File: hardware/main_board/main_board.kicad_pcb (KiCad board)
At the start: 2 copper layers, 14 parts, among them J100 2x10 Male Pins, J2 2x10 Male Pins, J4 2x10 Male Pins, J5 2x10 Male Pins, J6 2x10 Male Pins, J7 2x10 Male Pins, U1 M0G3507QDGS32RQ1, U2 HiLetGo_ST7735R

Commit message: drew schematic
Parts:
- removed J100: 2x10 Male Pins, Connector_PinSocket_2.54mm:PinSocket_2x10_P2.54mm_Vertical
- removed TP1, TP110, TP2, TP3, TP4, TP5: GND, SamacSys_Parts:bettertestpoint2
- added C1: 0.47uF, Capacitor_SMD:C_0805_2012Metric, F.Cu at (139.0, 94.9)
- added C10: 1u, Capacitor_SMD:C_0805_2012Metric, F.Cu at (142.1, 53.9)
- added C11: 0u33, Capacitor_SMD:C_0805_2012Metric, F.Cu at (142.1, 56.9)
- added C12: 1u, Capacitor_SMD:C_0805_2012Metric, F.Cu at (142.1, 59.9)
- added C3: 10nF, Capacitor_SMD:C_0805_2012Metric, F.Cu at (139.0, 97.9)
- added C4: 10uF, Capacitor_SMD:C_0805_2012Metric, F.Cu at (139.0, 100.9)
- added C5: 0.1uF, Capacitor_SMD:C_0805_2012Metric, F.Cu at (139.0, 103.9)
- added D1: RUN_LED, 445L:LED_D5.0mm, F.Cu at (143.7, 97.2)
- added D2: PWR_LED, 445L:LED_D5.0mm, F.Cu at (151.2, 97.2)
- added IC2: LM4890M_NOPB, 445L:ti_LM4890M_NOPB, F.Cu at (148.6, 55.6)
- added J1: Conn_01x06_Pin, Connector_PinHeader_2.54mm:PinHeader_1x06_P2.54mm_Vertical, F.Cu at (143.5, 103.2)
- added J3: 2x10 Male Pins, Connector_PinSocket_2.54mm:PinSocket_2x10_P2.54mm_Vertical, F.Cu at (95.9, 95.7)
- added J8: UJC-H-G-SMT-1-P6-TR, SamacSys_Parts:UJCHGSMT1P6TR, F.Cu at (146.8, 74.6)
- added J9: AudioJack, 445L:Jack_3.5mm_CUI_SJ1-3523N_Horizontal, F.Cu at (160.2, 45.3)
- added R1: 10k, Capacitor_SMD:C_0805_2012Metric, F.Cu at (139.0, 106.9)
- added R11: 5k1, Capacitor_SMD:C_0805_2012Metric, F.Cu at (142.1, 81.3)
- added R12: 5k1, Capacitor_SMD:C_0805_2012Metric, F.Cu at (142.1, 84.3)
- added R14: 20k, Capacitor_SMD:C_0805_2012Metric, F.Cu at (142.1, 62.9)
- added R15: 20k, Capacitor_SMD:C_0805_2012Metric, F.Cu at (142.1, 65.9)
- added R2: 10k, Capacitor_SMD:C_0805_2012Metric, F.Cu at (139.0, 109.9)
- added R3: 10k, Capacitor_SMD:C_0805_2012Metric, F.Cu at (157.9, 70.9)
- added R4: 47k, Capacitor_SMD:C_0805_2012Metric, F.Cu at (139.0, 113.0)
- added R5: 10k, Capacitor_SMD:C_0805_2012Metric, F.Cu at (157.9, 73.9)
- added R7: 470, Resistor_SMD:R_0805_2012Metric, F.Cu at (155.4, 111.0)
- added R8: 470, Resistor_SMD:R_0805_2012Metric, F.Cu at (155.4, 113.9)
- added SW1: RST, 445L:SW_PUSH_6mm, F.Cu at (147.9, 103.0)
- J2: value 2x10 Male Pins -> AudioJack; footprint Connector_PinSocket_2.54mm:PinSocket_2x10_P2.54mm_Vertical -> 445L:Jack_3.5mm_CUI_SJ1-3523N_Horizontal
- moved U1 71.9 mm to (149.5, 111.8)
- moved J2 68.7 mm to (146.7, 45.3)
- moved J6 47.8 mm to (123.4, 95.7)
- moved J5 35.4 mm to (132.5, 95.7)
- moved U2 26.8 mm to (114.5, 64.0)
- moved J7 22.5 mm to (105.1, 95.7)
- moved J4 14.6 mm to (114.2, 95.7)
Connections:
- net PA5/HFXIN renamed /MCU/SPI0.MOSI
- J4 pad 10: /Periph Board 3/CS -> /MCU/CS_{P2}
- J4 pad 11: /Periph Board 3/S0 -> /MCU/S0
- J4 pad 12: /Periph Board 3/S0 -> /MCU/S0
- J4 pad 13: /Periph Board 3/S1 -> /MCU/S1
- J4 pad 14: /Periph Board 3/S1 -> /MCU/S1
- J4 pad 15: /Periph Board 3/S2 -> /MCU/S2
- J4 pad 16: /Periph Board 3/S2 -> /MCU/S2
- J4 pad 17: /Periph Board 3/S3 -> /MCU/S3
- J4 pad 18: /Periph Board 3/S3 -> /MCU/S3
- J4 pad 5: /Periph Board 3/SCK -> /MCU/SPI0.SCK
- J4 pad 6: /Periph Board 3/SCK -> /MCU/SPI0.SCK
- J4 pad 7: /Periph Board 3/MISO -> /MCU/SPI0.MISO
- J4 pad 8: /Periph Board 3/MISO -> /MCU/SPI0.MISO
- J4 pad 9: /Periph Board 3/CS -> /MCU/CS_{P2}
- J5 pad 10: /Periph Board 4/CS -> /MCU/CS_{P3}
- J5 pad 11: /Periph Board 4/S0 -> /MCU/S0
- J5 pad 12: /Periph Board 4/S0 -> /MCU/S0
- J5 pad 13: /Periph Board 4/S1 -> /MCU/S1
- J5 pad 14: /Periph Board 4/S1 -> /MCU/S1
- J5 pad 15: /Periph Board 4/S2 -> /MCU/S2
- J5 pad 16: /Periph Board 4/S2 -> /MCU/S2
- J5 pad 17: /Periph Board 4/S3 -> /MCU/S3
- J5 pad 18: /Periph Board 4/S3 -> /MCU/S3
- J5 pad 5: /Periph Board 4/SCK -> /MCU/SPI0.SCK
- J5 pad 6: /Periph Board 4/SCK -> /MCU/SPI0.SCK
- J5 pad 7: /Periph Board 4/MISO -> /MCU/SPI0.MISO
- J5 pad 8: /Periph Board 4/MISO -> /MCU/SPI0.MISO
- J5 pad 9: /Periph Board 4/CS -> /MCU/CS_{P3}
- J6 pad 10: /Periph Board 5/CS -> /MCU/CS_{P4}
- J6 pad 11: /Periph Board 5/S0 -> /MCU/S0
- J6 pad 12: /Periph Board 5/S0 -> /MCU/S0
- J6 pad 13: /Periph Board 5/S1 -> /MCU/S1
- J6 pad 14: /Periph Board 5/S1 -> /MCU/S1
- J6 pad 15: /Periph Board 5/S2 -> /MCU/S2
- J6 pad 16: /Periph Board 5/S2 -> /MCU/S2
- J6 pad 17: /Periph Board 5/S3 -> /MCU/S3
- J6 pad 18: /Periph Board 5/S3 -> /MCU/S3
- J6 pad 5: /Periph Board 5/SCK -> /MCU/SPI0.SCK
- J6 pad 6: /Periph Board 5/SCK -> /MCU/SPI0.SCK
- J6 pad 7: /Periph Board 5/MISO -> /MCU/SPI0.MISO
- J6 pad 8: /Periph Board 5/MISO -> /MCU/SPI0.MISO
- J6 pad 9: /Periph Board 5/CS -> /MCU/CS_{P4}
- J7 pad 10: /Periph Board 6/CS -> /MCU/CS_{P5}
- J7 pad 11: /Periph Board 6/S0 -> /MCU/S0
- J7 pad 12: /Periph Board 6/S0 -> /MCU/S0
- J7 pad 13: /Periph Board 6/S1 -> /MCU/S1
- J7 pad 14: /Periph Board 6/S1 -> /MCU/S1
- J7 pad 15: /Periph Board 6/S2 -> /MCU/S2
- J7 pad 16: /Periph Board 6/S2 -> /MCU/S2
- J7 pad 17: /Periph Board 6/S3 -> /MCU/S3
- J7 pad 18: /Periph Board 6/S3 -> /MCU/S3
- J7 pad 5: /Periph Board 6/SCK -> /MCU/SPI0.SCK
- J7 pad 6: /Periph Board 6/SCK -> /MCU/SPI0.SCK
- J7 pad 7: /Periph Board 6/MISO -> /MCU/SPI0.MISO
- J7 pad 8: /Periph Board 6/MISO -> /MCU/SPI0.MISO
- J7 pad 9: /Periph Board 6/CS -> /MCU/CS_{P5}
- U1 pad 1: PA26 -> unconnected-(U1-PA26/A0_1-Pad1)
- U1 pad 10: PA3 -> /MCU/CS_{P2}
- U1 pad 11: PA4 -> /MCU/SPI0.MISO
- U1 pad 13: PA6/HFXOUT -> /MCU/SPI0.SCK
- U1 pad 14: PA7 -> /LCD/LCD_DC
- U1 pad 15: PA8/SPI0_CS0 -> /MCU/RUN_LED
- U1 pad 16: PA9 -> /LCD/CS_{LCD}
- U1 pad 17: PA10 -> /MCU/S0
- U1 pad 18: PA11/SPI0_SCK -> /MCU/S1
- U1 pad 19: PA12 -> /MCU/S2
- U1 pad 2: PA27/SPI1_CS1 -> unconnected-(U1-PA27/RTC_OUT/A0_0-Pad2)
- U1 pad 20: PA13/TFT_D/C -> /MCU/S3
- U1 pad 21: PA14/SPI0_PICO -> /Audio IO/ADC_IN
- U1 pad 22: PA15/DACOUT -> /Audio IO/DAC_OUT
- U1 pad 23: PA16/SPI1_POCI -> /LCD/SPI1.MISO
- U1 pad 24: PA17/SPI1_CLK -> /LCD/SPI1.SCK
- U1 pad 25: PA18/SPI1_PICO/BSL_Invoke -> /MCU/BSL_INVOKE
- U1 pad 26: SWDIO -> /MCU/SWDIO
- U1 pad 27: SWCLK -> /MCU/SWCLK
- U1 pad 28: PA21 -> unconnected-(U1-PA21/A1_7/VREF--Pad28)
- U1 pad 29: PA22 -> /MCU/CS_{P5}
- U1 pad 30: PA23 -> /MCU/CS_{P4}
- U1 pad 31: PA24/TFT_RESET -> /MCU/CS_{P3}
- U1 pad 32: PA25/SPI1_CS3 -> /LCD/CS_{SD}
- U1 pad 6: NRST -> /MCU/NRST
- U1 pad 9: PA2 -> /MCU/CS_{P1}
- U2 pad 1: unconnected-(U2-GND-Pad1) -> GND
- U2 pad 10: unconnected-(U2-TFT_CS-Pad10) -> /LCD/CS_{LCD}
- U2 pad 11: unconnected-(U2-SDCSCK-Pad11) -> /LCD/SPI1.SCK
- U2 pad 12: unconnected-(U2-SDC_MISO-Pad12) -> /LCD/SPI1.MISO
- U2 pad 13: unconnected-(U2-SDC_MOSI-Pad13) -> /LCD/SPI1.MOSI
- U2 pad 14: unconnected-(U2-SDC_CS-Pad14) -> /LCD/CS_{SD}
- U2 pad 15: unconnected-(U2-LED+-Pad15) -> +3V3
- U2 pad 16: unconnected-(U2-LED--Pad16) -> GND
- U2 pad 2: unconnected-(U2-VCC-Pad2) -> +3V3
- U2 pad 6: unconnected-(U2-RESET-Pad6) -> +3V3
- U2 pad 7: unconnected-(U2-TFTDC-Pad7) -> /LCD/LCD_DC
- U2 pad 8: unconnected-(U2-TFTMOSI-Pad8) -> /LCD/SPI1.MOSI
- U2 pad 9: unconnected-(U2-TFTSCK-Pad9) -> /LCD/SPI1.SCK

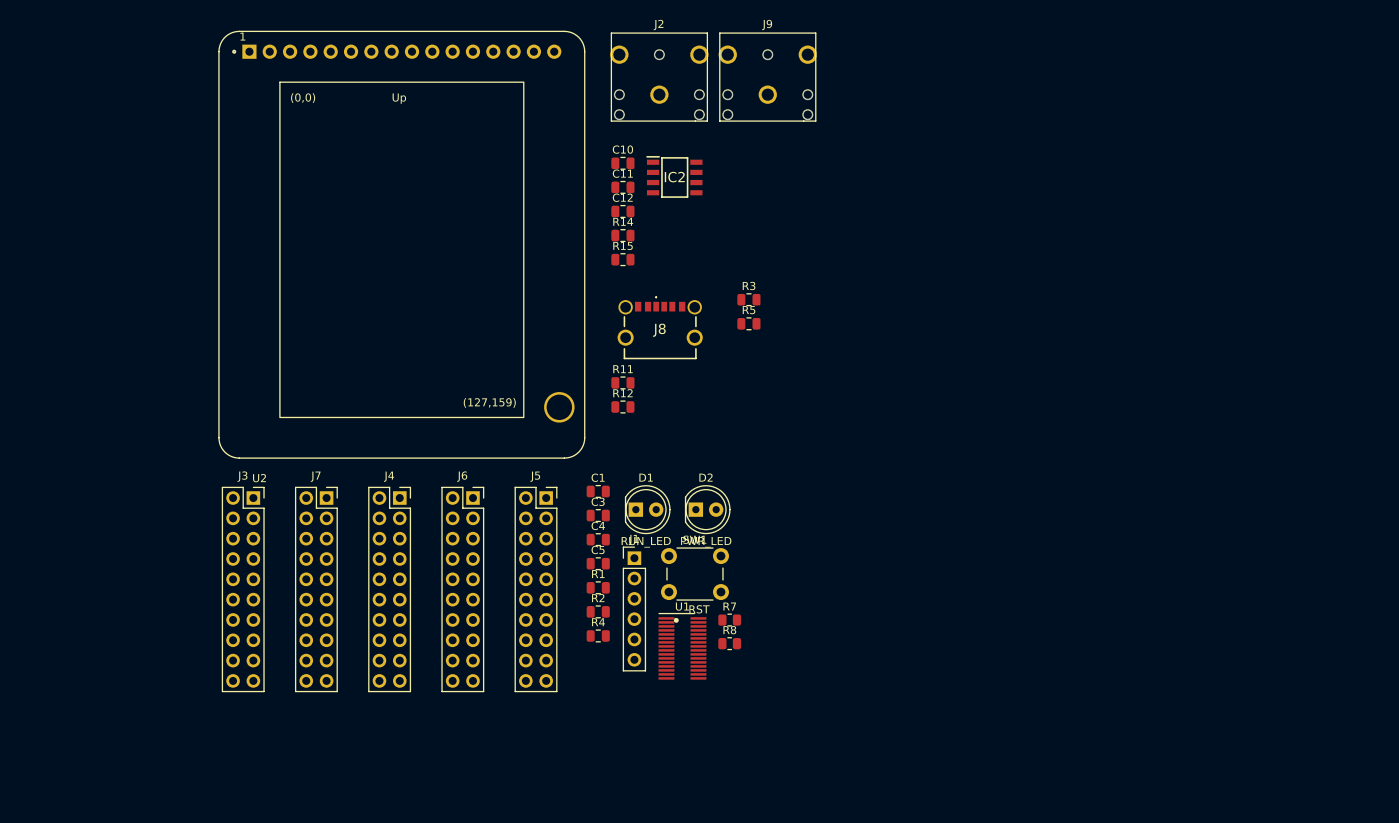
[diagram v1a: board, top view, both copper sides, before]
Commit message: port to i2c for both boards. periph board passes drc
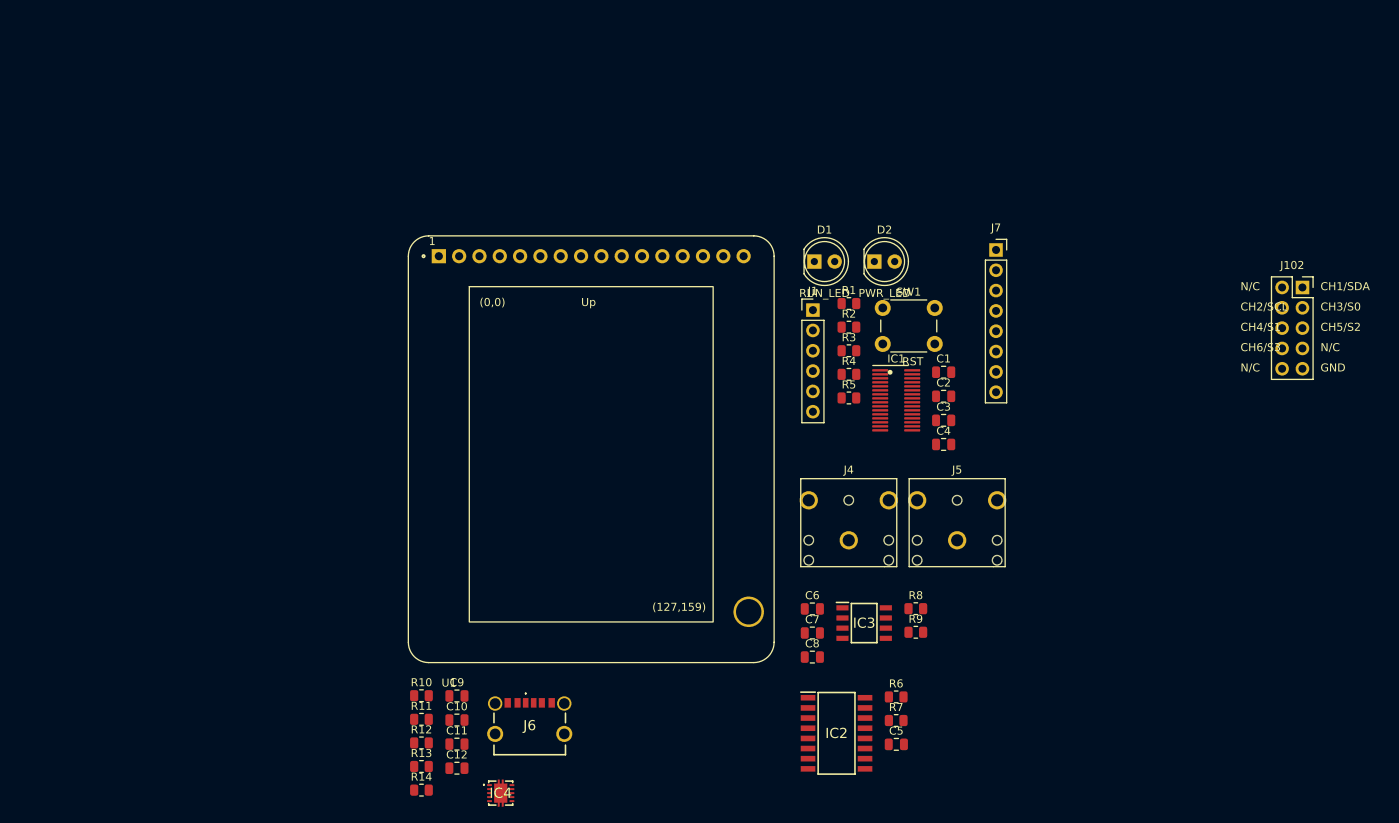
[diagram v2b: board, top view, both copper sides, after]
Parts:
- removed J2, J9: AudioJack, 445L:Jack_3.5mm_CUI_SJ1-3523N_Horizontal
- removed J3: 2x10 Male Pins, Connector_PinSocket_2.54mm:PinSocket_2x10_P2.54mm_Vertical
- removed J8: UJC-H-G-SMT-1-P6-TR, SamacSys_Parts:UJCHGSMT1P6TR
- removed R15: 20k, Capacitor_SMD:C_0805_2012Metric
- removed U2: HiLetGo_ST7735R, 445L:hiletgo_st7735r
- added C2: 10nF, Capacitor_SMD:C_0805_2012Metric, F.Cu at (182.2, 83.0)
- added C6: 1u, Capacitor_SMD:C_0805_2012Metric, F.Cu at (165.8, 109.6)
- added C7: 0u33, Capacitor_SMD:C_0805_2012Metric, F.Cu at (165.8, 112.6)
- added C8: 1u, Capacitor_SMD:C_0805_2012Metric, F.Cu at (165.8, 115.6)
- added C9: 10u, Capacitor_SMD:C_0805_2012Metric, F.Cu at (121.3, 120.5)
- added IC1: M0G3507QDGS32RQ1, 445L:generic_VSSOP_0.5mm, F.Cu at (176.3, 80.8)
- added IC3: LM4890M_NOPB, 445L:ti_LM4890M_NOPB, F.Cu at (172.3, 111.3)
- added IC4: TPS63000IDRCRQ1, SamacSys_Parts:TPS63000IDRCRQ1, F.Cu at (126.8, 132.6)
- added J102: 2x5 Socket Pins, Connector_PinSocket_2.54mm:PinSocket_2x05_P2.54mm_Vertical, F.Cu at (227.0, 69.4)
- added R10: 100, Resistor_SMD:R_0805_2012Metric, F.Cu at (116.9, 120.4)
- added R13: 5k1, Resistor_SMD:R_0805_2012Metric, F.Cu at (116.9, 129.3)
- added R6: 10k, Resistor_SMD:R_0805_2012Metric, F.Cu at (176.3, 120.6)
- added R9: 20k, Resistor_SMD:R_0805_2012Metric, F.Cu at (178.7, 112.5)
- C10: value 1u -> 10u
- C11: value 0u33 -> 10u
- C12: value 1u -> u1
- C3: value 10nF -> 10uF
- C4: value 10uF -> 0.1uF
- C5: value 0.1uF -> 1u
- IC2: value LM4890M_NOPB -> SN74HC157NSR; footprint 445L:ti_LM4890M_NOPB -> SamacSys_Parts:SOIC127P780X200-16N
- J4, J5: value 2x10 Male Pins -> AudioJack; footprint Connector_PinSocket_2.54mm:PinSocket_2x10_P2.54mm_Vertical -> 445L:Jack_3.5mm_CUI_SJ1-3523N_Horizontal
- J6: value 2x10 Male Pins -> UJC-H-G-SMT-1-P6-TR; footprint Connector_PinSocket_2.54mm:PinSocket_2x10_P2.54mm_Vertical -> SamacSys_Parts:UJCHGSMT1P6TR
- J7: value 2x10 Male Pins -> 1x8 Male Pins; footprint Connector_PinSocket_2.54mm:PinSocket_2x10_P2.54mm_Vertical -> Connector_PinSocket_2.54mm:PinSocket_1x08_P2.54mm_Vertical
- R1, R12, R2: footprint Capacitor_SMD:C_0805_2012Metric -> Resistor_SMD:R_0805_2012Metric
- R11: value 5k1 -> 1M; footprint Capacitor_SMD:C_0805_2012Metric -> Resistor_SMD:R_0805_2012Metric
- R14: value 20k -> 200k; footprint Capacitor_SMD:C_0805_2012Metric -> Resistor_SMD:R_0805_2012Metric
- R3: value 10k -> 47k; footprint Capacitor_SMD:C_0805_2012Metric -> Resistor_SMD:R_0805_2012Metric
- R4: value 47k -> 470; footprint Capacitor_SMD:C_0805_2012Metric -> Resistor_SMD:R_0805_2012Metric
- R5: value 10k -> 470; footprint Capacitor_SMD:C_0805_2012Metric -> Resistor_SMD:R_0805_2012Metric
- R7: value 470 -> 10k
- R8: value 470 -> 20k
- U1: value M0G3507QDGS32RQ1 -> HiLetGo_ST7735R; footprint 445L:generic_VSSOP_0.5mm -> 445L:hiletgo_st7735r
- moved J7 89.2 mm to (188.7, 64.7)
- moved R14 73.8 mm to (116.9, 132.2)
- moved C10 72.6 mm to (121.3, 123.5)
- moved C11 72.6 mm to (121.3, 126.5)
- moved C12 72.6 mm to (121.3, 129.5)
- moved IC2 72.4 mm to (168.8, 125.1)
- moved J4 56.4 mm to (170.3, 101.0)
- moved J5 51.6 mm to (183.9, 101.0)
- moved R11 49.0 mm to (116.9, 123.4)
- moved R12 49.0 mm to (116.9, 126.3)
- moved R2 47.4 mm to (170.3, 74.3)
- moved R1 47.4 mm to (170.3, 71.4)
- moved C1 45.7 mm to (182.2, 80.0)
- moved R4 45.3 mm to (170.3, 80.2)
- moved C3 44.8 mm to (182.2, 86.0)
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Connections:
- C1 pad 1: Net-(U1-VCORE) -> Net-(IC1-VCORE)
- C10 pad 1: GND -> +3V3
- C10 pad 2: +5V -> GNDPWR
- C11 pad 1: /Audio IO/DAC_OUT -> +3V3
- C11 pad 2: Net-(C11-Pad2) -> GNDPWR
- C12 pad 1: Net-(IC2-+IN) -> Net-(IC4-EN)
- C3 pad 1: /MCU/NRST -> +3V3
- C5 pad 1: +3V3 -> Net-(IC2-VCC)
- IC2 pad 1: GND -> /Encoders & Buttons/ENC_TOGGLE
- IC2 pad 2: Net-(IC2-+IN) -> /Encoders & Buttons/ENC1.SW
- IC2 pad 3: Net-(IC2-+IN) -> /Encoders & Buttons/ENC2.SW
- IC2 pad 4: Net-(IC2--IN) -> /Encoders & Buttons/ENC.SW
- IC2 pad 5: Net-(IC2-VO_1) -> /Encoders & Buttons/ENC1.DT
- IC2 pad 6: +5V -> /Encoders & Buttons/ENC2.DT
- IC2 pad 7: GND -> /Encoders & Buttons/ENC.DT
- IC2 pad 8: unconnected-(IC2-VO2-Pad8) -> GND
- J7 pad 1: +3V3 -> +5V
- J7 pad 2: +3V3 -> /Peripheral Boards/SDA
- J7 pad 3: +5V -> /Peripheral Boards/SCL
- J7 pad 4: +5V -> /MCU/S0
- J7 pad 5: /MCU/SPI0.SCK -> /MCU/S1
- J7 pad 6: /MCU/SPI0.SCK -> /MCU/S2
- J7 pad 7: /MCU/SPI0.MISO -> /MCU/S3
- J7 pad 8: /MCU/SPI0.MISO -> GND
- R1 pad 1: PA1 -> /MCU/I2C0.SCL
- R11 pad 1: Net-(J8-CC2) -> +3V3
- R11 pad 2: GND -> Net-(IC4-FB)
- R12 pad 1: Net-(J8-CC1) -> Net-(J6-CC2)
- R14 pad 1: Net-(C11-Pad2) -> Net-(IC4-FB)
- R14 pad 2: Net-(IC2--IN) -> GND
- R2 pad 1: PA0 -> /MCU/I2C0.SDA
- R3 pad 1: /Encoders & Buttons/ENC1.SW -> +3V3
- R3 pad 2: +3V3 -> /MCU/NRST
- R4 pad 1: +3V3 -> /MCU/RUN_LED
- R4 pad 2: /MCU/NRST -> Net-(D1-A)
- R5 pad 1: /Encoders & Buttons/ENC2.SW -> +3V3
- R5 pad 2: +3V3 -> Net-(D2-A)
- R7 pad 1: /MCU/RUN_LED -> /Encoders & Buttons/ENC2.SW
- R7 pad 2: Net-(D1-A) -> +3V3
- R8 pad 1: +3V3 -> Net-(C7-Pad2)
- R8 pad 2: Net-(D2-A) -> Net-(IC3--IN)
- U1 pad 1: unconnected-(U1-PA26/A0_1-Pad1) -> GND
- U1 pad 10: /MCU/CS_{P2} -> /LCD/CS_LCD
- U1 pad 11: /MCU/SPI0.MISO -> /LCD/SPI0.SCK
- U1 pad 12: /MCU/SPI0.MOSI -> /LCD/SPI0.MISO
- U1 pad 13: /MCU/SPI0.SCK -> /LCD/SPI0.MOSI
- U1 pad 14: /LCD/LCD_DC -> /LCD/CS_SD
- U1 pad 15: /MCU/RUN_LED -> +3V3
- U1 pad 16: /LCD/CS_{LCD} -> GND
- U1 pad 2: unconnected-(U1-PA27/RTC_OUT/A0_0-Pad2) -> +3V3
- U1 pad 3: Net-(U1-VCORE) -> unconnected-(U1-Pin3-Pad3)
- U1 pad 4: PA0 -> unconnected-(U1-Pin4-Pad4)
- U1 pad 5: PA1 -> unconnected-(U1-Pin5-Pad5)
- U1 pad 6: /MCU/NRST -> +3V3
- U1 pad 7: +3V3 -> /LCD/LCD_DC
- U1 pad 8: GND -> /LCD/SPI0.MOSI
- U1 pad 9: /MCU/CS_{P1} -> /LCD/SPI0.SCK
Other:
- board text added: "CH1/SDA"
- board text added: "CH2/SCL"
- board text added: "CH3/S0"
- board text added: "CH4/S1"
- board text added: "CH5/S2"
- board text added: "CH6/S3"
- board text added: "GND"
- board text added: "N/C"
